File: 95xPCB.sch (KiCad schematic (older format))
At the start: 132 parts

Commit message: v1
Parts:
- added D? (x31): S0D-123, symbol Device:D_Small
- added MX? (x31): MX-NoLED, symbol MX_Alps_Hybrid:MX-NoLED
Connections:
- wire segments 102 -> 220
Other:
- moved on the sheet: D?

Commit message: v1
This time we have an actual description:
keyboard has a USB-C connector currently being developed and a last resort 6 pin board. Removed key switches. (WILL BE BACK, just in a different way)
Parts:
- removed D? (x90): S0D-123, symbol Device:D_Small
- removed MX? (x90): MX-NoLED, symbol MX_Alps_Hybrid:MX-NoLED
- added F?: 500m, symbol Device:Polyfuse_Small
- added J?: AVR-ISP-6, symbol Connector:AVR-ISP-6
- added R? (x2): 5.1k, symbol Device:R_Small
- added USB?: HRO-TYPE-C-31-M-12, symbol Type-C:HRO-TYPE-C-31-M-12
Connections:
- net labels added: MISO, MOSI, RESET, SCK, VCC
- wire segments 220 -> 75
- no-connect marks 0 -> 2
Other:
- moved on the sheet: R?, SW?

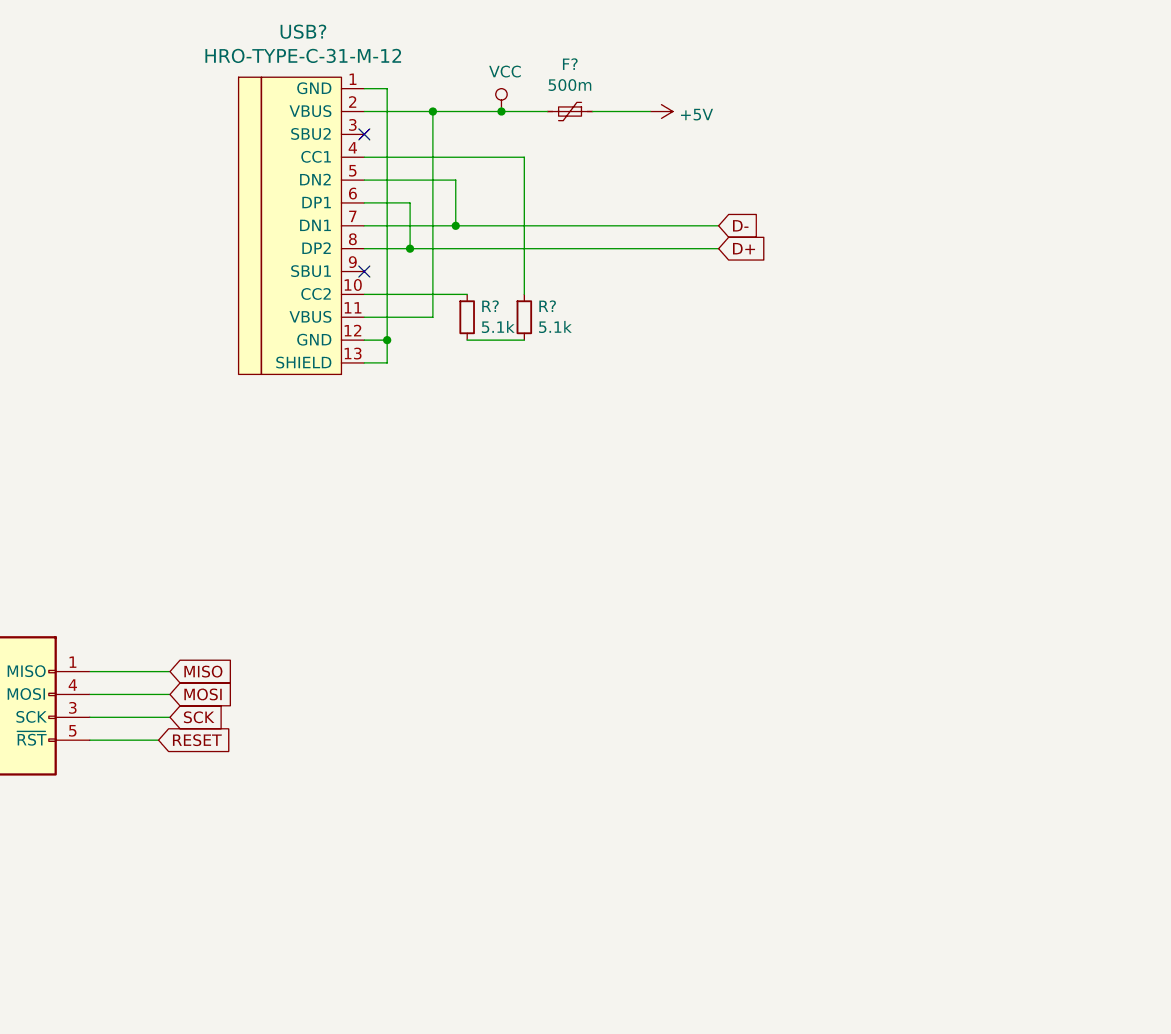
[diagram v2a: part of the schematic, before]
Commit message: v1a
USB-C connector finished, refining circuitry.
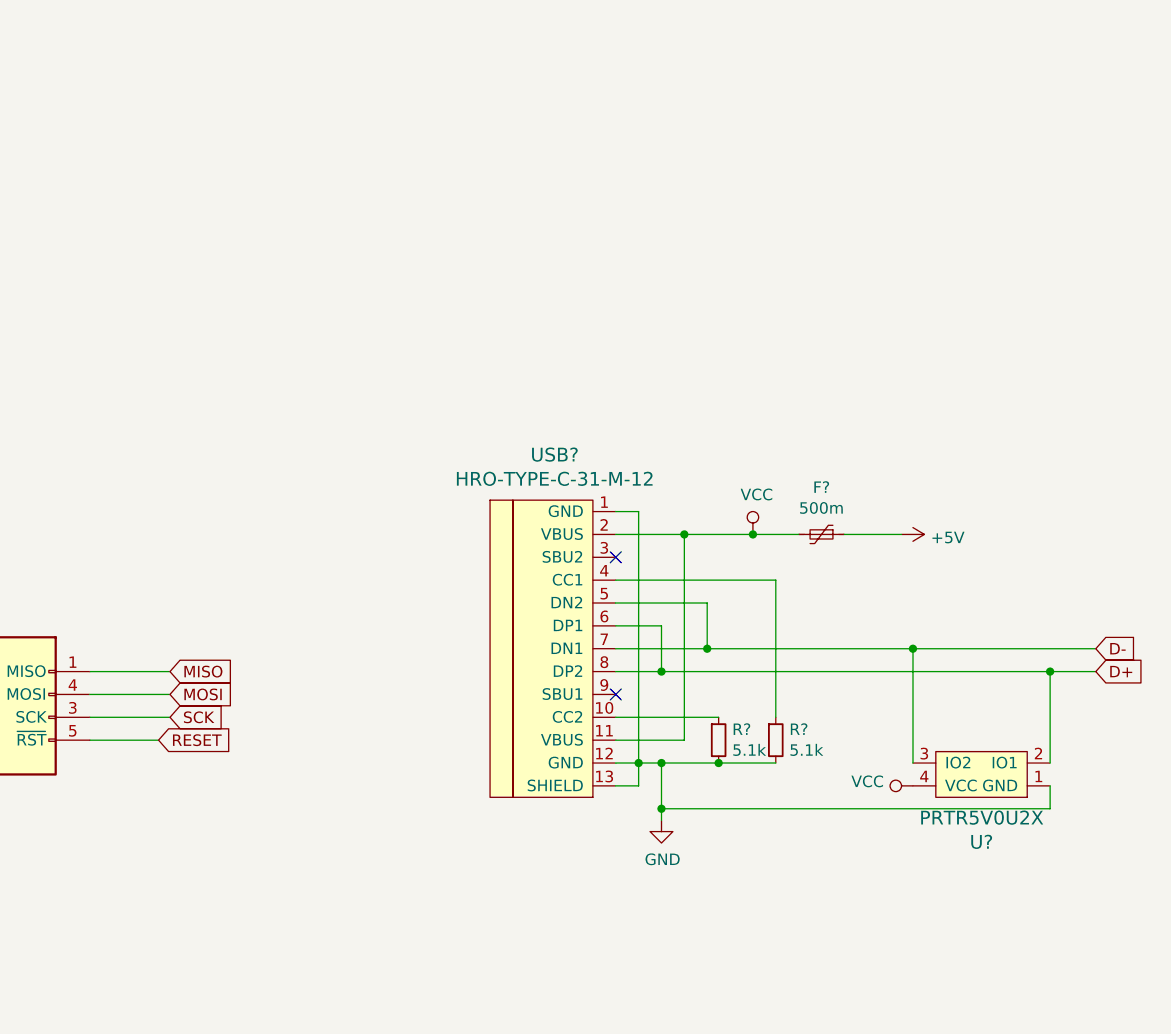
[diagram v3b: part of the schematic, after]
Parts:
- added U?: PRTR5V0U2X, symbol random-keyboard-parts:PRTR5V0U2X
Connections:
- net D+: now also U?.2 (IO1)
- net D-: now also U?.3 (IO2)
- net GND: now also R?.2, R?.2, USB?.1 (GND), USB?.12 (GND), USB?.13 (SHIELD), U?.1 (GND)
- net VCC: now also U?.4 (VCC)
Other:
- moved on the sheet: F?, R?, USB?
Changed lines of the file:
@@
 L Type-C:HRO-TYPE-C-31-M-12 USB?
 U 1 1 63863458
-P 18700 -700
-F 0 "USB?" H 18533 97  60  0000 C CNN
-F 1 "HRO-TYPE-C-31-M-12" H 18533 -9  60  0000 C CNN
-F 2 "" H 18700 -700 60  0001 C CNN
-F 3 "" H 18700 -700 60  0001 C CNN
-	1    18700 -700
+P 19800 1150
+F 0 "USB?" H 19633 1947 60  0000 C CNN
+F 1 "HRO-TYPE-C-31-M-12" H 19633 1841 60  0000 C CNN
+F 2 "" H 19800 1150 60  0001 C CNN
+F 3 "" H 19800 1150 60  0001 C CNN
+	1    19800 1150
 	1    0    0    -1
 $EndComp
-Text GLabel 20350 -650 2    50   Input ~ 0
+Text GLabel 22000 1200 2    50   Input ~ 0
 D-
-Text GLabel 20350 -550 2    50   Input ~ 0
+Text GLabel 22000 1300 2    50   Input ~ 0
 D+
 Wire Wire Line
-	18800 -750 19000 -750
+	19900 1100 20100 1100
 Wire Wire Line
-	19000 -750 19000 -550
-Connection ~ 19000 -550
+	20100 1100 20100 1300
+Connection ~ 20100 1300
 Wire Wire Line
-	19000 -550 18800 -550
+	19900 1000 20300 1000
 Wire Wire Line
-	18800 -850 19200 -850
+	20300 1000 20300 1200
+Connection ~ 20300 1200
 Wire Wire Line
-	19200 -850 19200 -650
-Connection ~ 19200 -650
+	19900 600  20000 600
 Wire Wire Line
-	19200 -650 18800 -650
+	20000 600  20000 1700
 Wire Wire Line
-	18800 -1250 18900 -1250
+	20000 1800 19900 1800
 Wire Wire Line
-	18900 -1250 18900 -150
+	19900 1700 20000 1700
+Connection ~ 20000 1700
 Wire Wire Line
-	18900 -50  18800 -50
+	20000 1700 20000 1800
 Wire Wire Line
-	18800 -150 18900 -150
-Connection ~ 18900 -150
+	19900 1600 20200 1600
 Wire Wire Line
-	18900 -150 18900 -50
+	20200 1600 20200 700
 Wire Wire Line
-	18800 -250 19100 -250
-Wire Wire Line
-	19100 -250 19100 -1150
-Wire Wire Line
-	19100 -1150 18800 -1150
+	20200 700  19900 700
 $Comp
 L power:VCC #PWR?
 U 1 1 6386DE51
-P 19400 -1150
-F 0 "#PWR?" H 19400 -1300 50  0001 C CNN
-F 1 "VCC" H 19417 -977 50  0000 C CNN
-F 2 "" H 19400 -1150 50  0001 C CNN
-F 3 "" H 19400 -1150 50  0001 C CNN
-	1    19400 -1150
+P 20500 700
+F 0 "#PWR?" H 20500 550 50  0001 C CNN
+F 1 "VCC" H 20517 873 50  0000 C CNN
+F 2 "" H 20500 700 50  0001 C CNN
+F 3 "" H 20500 700 50  0001 C CNN
+	1    20500 700
 	1    0    0    -1
 $EndComp
 Wire Wire Line
-	19100 -1150 19400 -1150
-Connection ~ 19100 -1150
+	20200 700  20500 700
+Connection ~ 20200 700
 $Comp
 L Device:Polyfuse_Small F?
 U 1 1 63870A1C
-P 19700 -1150
-F 0 "F?" V 19495 -1150 50  0000 C CNN
-F 1 "500m" V 19586 -1150 50  0000 C CNN
-F 2 "" H 19750 -1350 50  0001 L CNN
-F 3 "~" H 19700 -1150 50  0001 C CNN
-	1    19700 -1150
+P 20800 700
+F 0 "F?" V 20595 700 50  0000 C CNN
+F 1 "500m" V 20686 700 50  0000 C CNN
+F 2 "" H 20850 500 50  0001 L CNN
+F 3 "~" H 20800 700 50  0001 C CNN
+	1    20800 700
 	0    1    1    0
 $EndComp
 Wire Wire Line
-	19400 -1150 19600 -1150
-Connection ~ 19400 -1150
+	20500 700  20700 700
+Connection ~ 20500 700
 $Comp
 L power:+5V #PWR?
 U 1 1 6387940F
-P 20050 -1150
-F 0 "#PWR?" H 20050 -1300 50  0001 C CNN
-F 1 "+5V" V 20065 -1022 50  0000 L CNN
-F 2 "" H 20050 -1150 50  0001 C CNN
-F 3 "" H 20050 -1150 50  0001 C CNN
-	1    20050 -1150
+P 21150 700
+F 0 "#PWR?" H 21150 550 50  0001 C CNN
+F 1 "+5V" V 21165 828 50  0000 L CNN
+F 2 "" H 21150 700 50  0001 C CNN
+F 3 "" H 21150 700 50  0001 C CNN
+	1    21150 700
 	0    1    1    0
 $EndComp
 Wire Wire Line
-	19800 -1150 20050 -1150
-NoConn ~ 18800 -1050
-NoConn ~ 18800 -450
+	20900 700  21150 700
+NoConn ~ 19900 800
+NoConn ~ 19900 1400
 $Comp
 L Device:R_Small R?
 U 1 1 6387F88A
-P 19500 -250
-F 0 "R?" H 19559 -204 50  0000 L CNN
-F 1 "5.1k" H 19559 -295 50  0000 L CNN
-F 2 "" H 19500 -250 50  0001 C CNN
-F 3 "~" H 19500 -250 50  0001 C CNN
-	1    19500 -250
+P 20600 1600
+F 0 "R?" H 20659 1646 50  0000 L CNN
+F 1 "5.1k" H 20659 1555 50  0000 L CNN
+F 2 "" H 20600 1600 50  0001 C CNN
+F 3 "~" H 20600 1600 50  0001 C CNN
+	1    20600 1600
 	1    0    0    -1
 $EndComp
 Wire Wire Line
-	19200 -650 20350 -650
+	20600 900  19900 900
 Wire Wire Line
-	19000 -550 20350 -550
+	20350 1500 19900 1500
 Wire Wire Line
-	19500 -950 18800 -950
-Wire Wire Line
-	19250 -350 18800 -350
-Wire Wire Line
-	19500 -150 19250 -150
+	20600 1700 20350 1700
 $Comp
 L Device:R_Small R?
 U 1 1 6389C842
-P 19250 -250
-F 0 "R?" H 19309 -204 50  0000 L CNN
-F 1 "5.1k" H 19309 -295 50  0000 L CNN
-F 2 "" H 19250 -250 50  0001 C CNN
-F 3 "~" H 19250 -250 50  0001 C CNN
-	1    19250 -250
+P 20350 1600
+F 0 "R?" H 20409 1646 50  0000 L CNN
+F 1 "5.1k" H 20409 1555 50  0000 L CNN
+F 2 "" H 20350 1600 50  0001 C CNN
+F 3 "~" H 20350 1600 50  0001 C CNN
+	1    20350 1600
 	1    0    0    -1
 $EndComp
 Wire Wire Line
-	19500 -950 19500 -350
+	20600 900  20600 1500
+Wire Wire Line
+	20000 1700 20100 1700
+Connection ~ 20350 1700
+$Comp
+L power:GND #PWR?
+U 1 1 6372ADC6
+P 20100 1950
+F 0 "#PWR?" H 20100 1700 50  0001 C CNN
+F 1 "GND" H 20105 1777 50  0000 C CNN
+F 2 "" H 20100 1950 50  0001 C CNN
+F 3 "" H 20100 1950 50  0001 C CNN
+	1    20100 1950
+	1    0    0    -1
+$EndComp
+Connection ~ 20100 1700
+Wire Wire Line
+	20100 1700 20350 1700
+Wire Wire Line
+	20100 1700 20100 1900
+Wire Wire Line
+	19900 1300 20100 1300
+Wire Wire Line
+	19900 1200 20300 1200
+Wire Wire Line
+	20300 1200 21200 1200
+$Comp
+L random-keyboard-parts:PRTR5V0U2X U?
+U 1 1 63743CC9
+P 21500 1750
+F 0 "U?" H 21500 2047 60  0000 C CNN
+F 1 "PRTR5V0U2X" H 21500 1941 60  0000 C CNN
+F 2 "" H 21500 1750 60  0001 C CNN
+F 3 "" H 21500 1750 60  0001 C CNN
+	1    21500 1750
+	-1   0    0    1
+$EndComp
+Wire Wire Line
+	21200 1700 21200 1200
+Connection ~ 21200 1200
+Wire Wire Line
+	21200 1200 22000 1200
+Wire Wire Line
+	20100 1300 21800 1300
+Wire Wire Line
+	21800 1700 21800 1300
+Connection ~ 21800 1300
+Wire Wire Line
+	21800 1300 22000 1300
+Wire Wire Line
+	21800 1800 21800 1900
+Wire Wire Line
+	21800 1900 20100 1900
+Connection ~ 20100 1900
+Wire Wire Line
+	20100 1900 20100 1950
+$Comp
+L power:VCC #PWR?
+U 1 1 637546F2
+P 21200 1800
+F 0 "#PWR?" H 21200 1650 50  0001 C CNN
+F 1 "VCC" V 21218 1927 50  0000 L CNN
+F 2 "" H 21200 1800 50  0001 C CNN
+F 3 "" H 21200 1800 50  0001 C CNN
+	1    21200 1800
+	0    -1   -1   0
+$EndComp
 $EndSCHEMATC

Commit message: v1a1
Redid reset switch. Next phase is the keyboard switch matrix. Yay.
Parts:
- removed SW?: SW_Push, symbol Switch:SW_Push
- added U?: SW_SQKG, symbol random-keyboard-parts:SW_SQKG
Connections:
- net GND: now also U?.2
- net RESET: now also U?.1
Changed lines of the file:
@@
 $EndDescr
 $Comp
-L power:+5V #PWR?
+L power:+5V #PWR0101
 U 1 1 63721B9F
 P 18850 3500
-F 0 "#PWR?" H 18850 3350 50  0001 C CNN
+F 0 "#PWR0101" H 18850 3350 50  0001 C CNN
 F 1 "+5V" H 18865 3673 50  0000 C CNN
 F 2 "" H 18850 3500 50  0001 C CNN
@@
 	18850 3700 18850 3500
 $Comp
-L power:GND #PWR?
+L power:GND #PWR0102
 U 1 1 63722F38
 P 18500 7300
-F 0 "#PWR?" H 18500 7050 50  0001 C CNN
+F 0 "#PWR0102" H 18500 7050 50  0001 C CNN
 F 1 "GND" H 18505 7127 50  0000 C CNN
 F 2 "" H 18500 7300 50  0001 C CNN
@@
 $EndComp
 $Comp
-L power:GND #PWR?
+L power:GND #PWR0103
 U 1 1 6372EBA5
 P 20700 6100
-F 0 "#PWR?" H 20700 5850 50  0001 C CNN
+F 0 "#PWR0103" H 20700 5850 50  0001 C CNN
 F 1 "GND" H 20705 5927 50  0000 C CNN
 F 2 "" H 20700 6100 50  0001 C CNN
@@
 	18350 5300 17750 5300
 $Comp
-L power:GND #PWR?
+L power:GND #PWR0104
 U 1 1 63737CC6
 P 17750 5750
-F 0 "#PWR?" H 17750 5500 50  0001 C CNN
+F 0 "#PWR0104" H 17750 5500 50  0001 C CNN
 F 1 "GND" H 17755 5577 50  0000 C CNN
 F 2 "" H 17750 5750 50  0001 C CNN
@@
 $EndComp
 $Comp
-L power:GND #PWR?
+L power:GND #PWR0105
 U 1 1 6373CA4C
 P 17350 6800
-F 0 "#PWR?" H 17350 6550 50  0001 C CNN
+F 0 "#PWR0105" H 17350 6550 50  0001 C CNN
 F 1 "GND" H 17355 6627 50  0000 C CNN
 F 2 "" H 17350 6800 50  0001 C CNN
@@
 $EndComp
 $Comp
-L power:+5V #PWR?
+L power:+5V #PWR0106
 U 1 1 6373DB7B
 P 17350 6300
-F 0 "#PWR?" H 17350 6150 50  0001 C CNN
+F 0 "#PWR0106" H 17350 6150 50  0001 C CNN
 F 1 "+5V" H 17365 6473 50  0000 C CNN
 F 2 "" H 17350 6300 50  0001 C CNN
@@
 	17350 6300 17350 6450
 $Comp
-L power:+5V #PWR?
+L power:+5V #PWR0107
 U 1 1 637452E3
 P 17650 4800
-F 0 "#PWR?" H 17650 4650 50  0001 C CNN
+F 0 "#PWR0107" H 17650 4650 50  0001 C CNN
 F 1 "+5V" H 17665 4973 50  0000 C CNN
 F 2 "" H 17650 4800 50  0001 C CNN
@@
 	17700 4500 17700 4550
 $Comp
-L power:GND #PWR?
+L power:GND #PWR0108
 U 1 1 63757699
 P 17350 4550
-F 0 "#PWR?" H 17350 4300 50  0001 C CNN
+F 0 "#PWR0108" H 17350 4300 50  0001 C CNN
 F 1 "GND" H 17355 4377 50  0000 C CNN
 F 2 "" H 17350 4550 50  0001 C CNN
@@
 	16250 2550 16250 2650
 $Comp
-L power:+5V #PWR?
+L power:+5V #PWR0109
 U 1 1 6375E019
 P 16250 2550
-F 0 "#PWR?" H 16250 2400 50  0001 C CNN
+F 0 "#PWR0109" H 16250 2400 50  0001 C CNN
 F 1 "+5V" H 16265 2723 50  0000 C CNN
 F 2 "" H 16250 2550 50  0001 C CNN
@@
 $EndComp
 Wire Wire Line
-	15800 3050 15800 3150
-Wire Wire Line
-	15600 3050 15800 3050
-$Comp
-L power:GND #PWR?
+	15350 3350 15550 3350
+$Comp
+L power:GND #PWR0110
 U 1 1 6375A6A4
-P 15600 3050
-F 0 "#PWR?" H 15600 2800 50  0001 C CNN
-F 1 "GND" H 15605 2877 50  0000 C CNN
-F 2 "" H 15600 3050 50  0001 C CNN
-F 3 "" H 15600 3050 50  0001 C CNN
-	1    15600 3050
-	1    0    0    -1
-$EndComp
-Wire Wire Line
-	16200 3150 16250 3150
-$Comp
-L Switch:SW_Push SW?
-U 1 1 63757FC2
-P 16000 3150
-F 0 "SW?" H 16000 3435 50  0000 C CNN
-F 1 "SW_Push" H 16000 3344 50  0000 C CNN
-F 2 "" H 16000 3350 50  0001 C CNN
-F 3 "~" H 16000 3350 50  0001 C CNN
-	1    16000 3150
+P 15350 3350
+F 0 "#PWR0110" H 15350 3100 50  0001 C CNN
+F 1 "GND" H 15355 3177 50  0000 C CNN
+F 2 "" H 15350 3350 50  0001 C CNN
+F 3 "" H 15350 3350 50  0001 C CNN
+	1    15350 3350
 	1    0    0    -1
 $EndComp
@@
 	17600 1500 17950 1500
 $Comp
-L power:+5V #PWR?
+L power:+5V #PWR0111
 U 1 1 637CEEF3
 P 17100 850
-F 0 "#PWR?" H 17100 700 50  0001 C CNN
+F 0 "#PWR0111" H 17100 700 50  0001 C CNN
 F 1 "+5V" H 17115 1023 50  0000 C CNN
 F 2 "" H 17100 850 50  0001 C CNN
@@
 	17100 850  17100 1000
 $Comp
-L power:GND #PWR?
+L power:GND #PWR0112
 U 1 1 637ECC94
 P 17100 2100
-F 0 "#PWR?" H 17100 1850 50  0001 C CNN
+F 0 "#PWR0112" H 17100 1850 50  0001 C CNN
 F 1 "GND" H 17105 1927 50  0000 C CNN
 F 2 "" H 17100 2100 50  0001 C CNN
@@
 	20200 700  19900 700
 $Comp
-L power:VCC #PWR?
+L power:VCC #PWR0113
 U 1 1 6386DE51
 P 20500 700
-F 0 "#PWR?" H 20500 550 50  0001 C CNN
+F 0 "#PWR0113" H 20500 550 50  0001 C CNN
 F 1 "VCC" H 20517 873 50  0000 C CNN
 F 2 "" H 20500 700 50  0001 C CNN
@@
 Connection ~ 20500 700
 $Comp
-L power:+5V #PWR?
+L power:+5V #PWR0114
 U 1 1 6387940F
 P 21150 700
-F 0 "#PWR?" H 21150 550 50  0001 C CNN
+F 0 "#PWR0114" H 21150 550 50  0001 C CNN
 F 1 "+5V" V 21165 828 50  0000 L CNN
 F 2 "" H 21150 700 50  0001 C CNN
@@
 Connection ~ 20350 1700
 $Comp
-L power:GND #PWR?
+L power:GND #PWR0115
 U 1 1 6372ADC6
 P 20100 1950
-F 0 "#PWR?" H 20100 1700 50  0001 C CNN
+F 0 "#PWR0115" H 20100 1700 50  0001 C CNN
 F 1 "GND" H 20105 1777 50  0000 C CNN
 F 2 "" H 20100 1950 50  0001 C CNN
@@
 	20100 1900 20100 1950
 $Comp
-L power:VCC #PWR?
+L power:VCC #PWR0116
 U 1 1 637546F2
 P 21200 1800
-F 0 "#PWR?" H 21200 1650 50  0001 C CNN
+F 0 "#PWR0116" H 21200 1650 50  0001 C CNN
 F 1 "VCC" V 21218 1927 50  0000 L CNN
 F 2 "" H 21200 1800 50  0001 C CNN
@@
 	0    -1   -1   0
 $EndComp
+$Comp
+L random-keyboard-parts:SW_SQKG U?
+U 1 1 6373FC2E
+P 15750 3000
+F 0 "U?" H 15800 3075 50  0000 C CNN
+F 1 "SW_SQKG" H 15800 2984 50  0000 C CNN
+F 2 "" H 15750 3000 50  0001 C CNN
+F 3 "" H 15750 3000 50  0001 C CNN
+	1    15750 3000
+	1    0    0    -1
+$EndComp
+Wire Wire Line
+	16050 3150 16250 3150
 $EndSCHEMATC
